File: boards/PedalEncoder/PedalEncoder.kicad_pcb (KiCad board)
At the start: 2 copper layers, 27 parts, among them J1 Pwr, J2 Control, J3 Switch, J4 ISP, J5 Pedal, J6 MIDI Out, Q1 BC547, U1 4069, U2 ATtiny2313V-10P, U3 L7805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

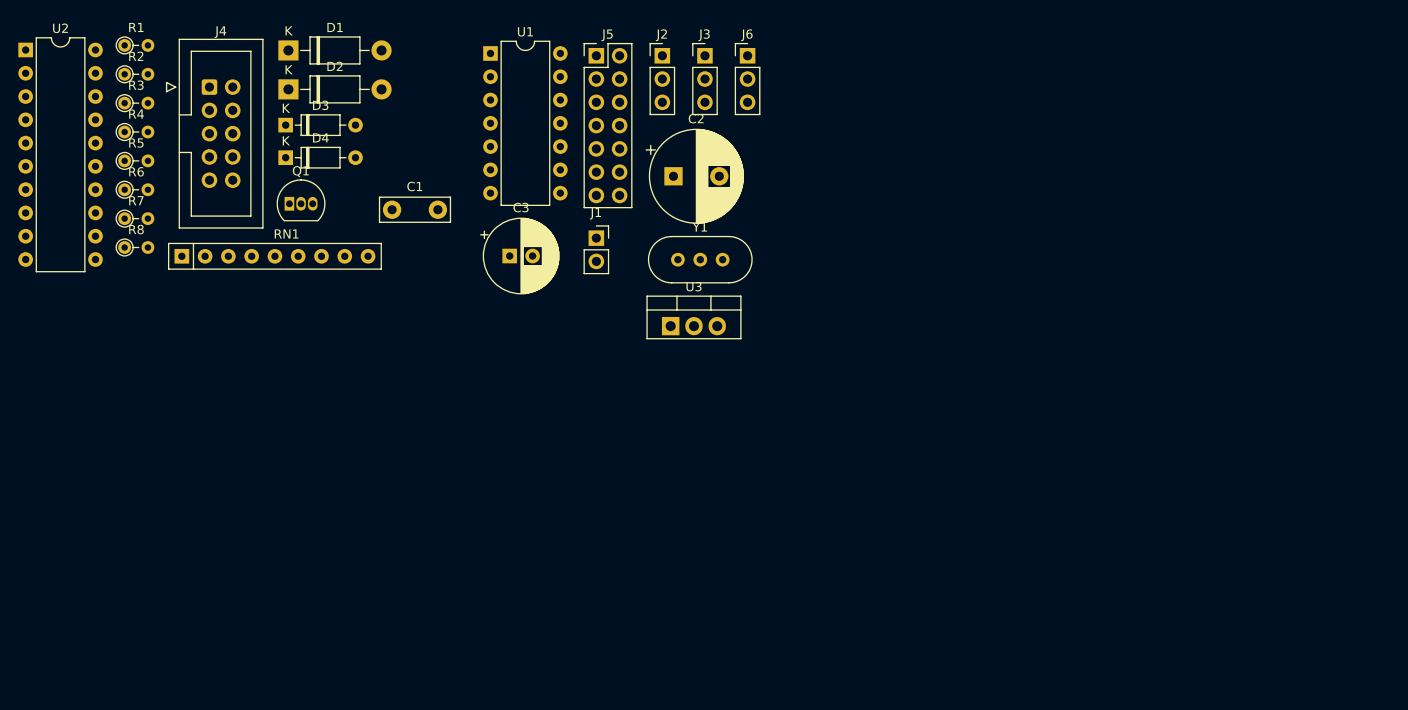
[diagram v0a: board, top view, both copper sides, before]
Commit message: Updated to KiCAD 8, fixed optocouplers for MIDI and added powersupplies
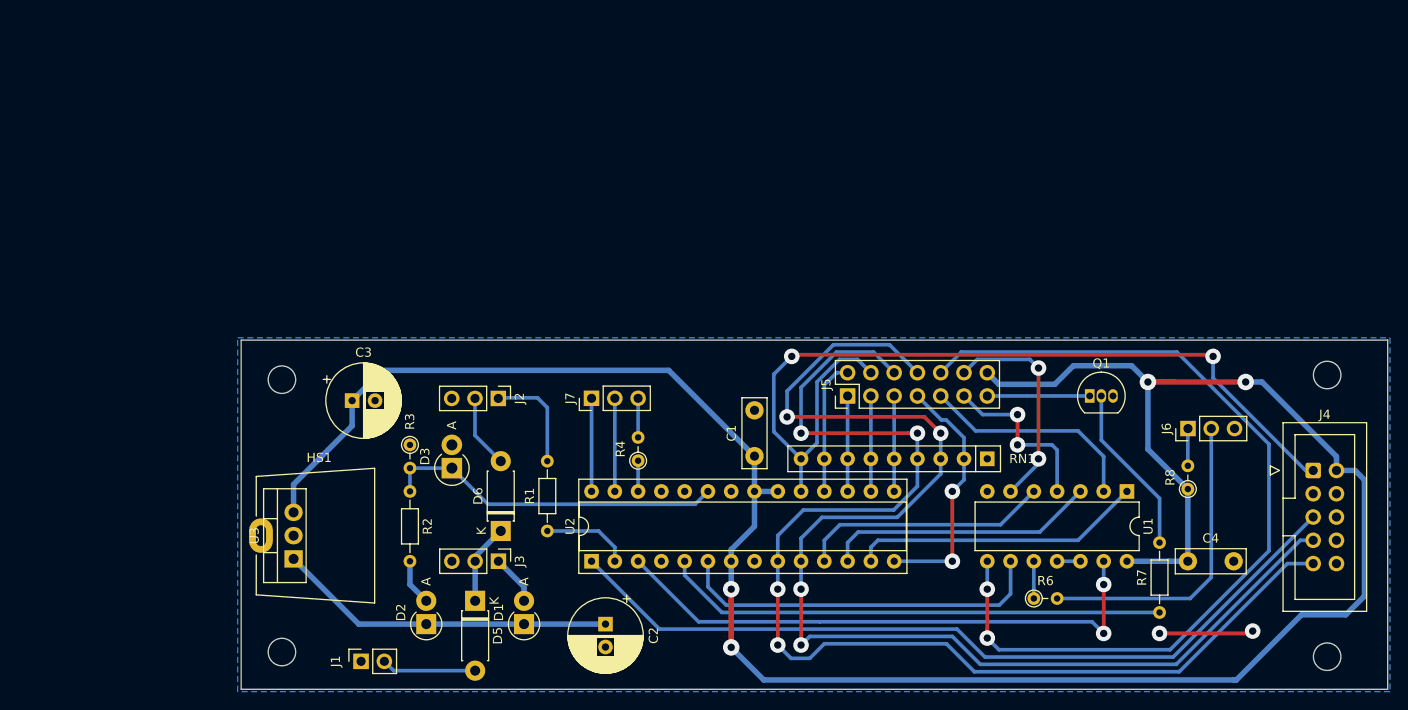
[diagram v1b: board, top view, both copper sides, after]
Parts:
- removed D4: 1N4148, Diode_THT:D_DO-35_SOD27_P7.62mm_Horizontal
- removed R5: 220, Resistor_THT:R_Axial_DIN0204_L3.6mm_D1.6mm_P2.54mm_Vertical
- removed Y1: 4Mhz, Crystal:Crystal_HC49-U-3Pin_Vertical
- added C4: 100nF, Capacitor_THT:C_Disc_D7.5mm_W2.5mm_P5.00mm, F.Cu at (173.3, 99.3)
- added D5: 1N4002, Diode_THT:D_DO-41_SOD81_P7.62mm_Horizontal, F.Cu at (95.5, 103.6)
- added D6: 1N4002, Diode_THT:D_DO-41_SOD81_P7.62mm_Horizontal, F.Cu at (98.3, 96.0)
- added H1: MountingHole, MountingHole:MountingHole_3mm, F.Cu at (74.4, 79.5)
- added H2: MountingHole, MountingHole:MountingHole_3mm, F.Cu at (74.4, 109.2)
- added H3: MountingHole, MountingHole:MountingHole_3mm, F.Cu at (188.5, 79.0)
- added H4: MountingHole, MountingHole:MountingHole_3mm, F.Cu at (188.5, 109.7)
- added HS1: Heatsink_Pad, Heatsink:Heatsink_AAVID_576802B03900G, F.Cu at (72.1, 96.5)
- added J7: I2C, Connector_PinHeader_2.54mm:PinHeader_1x03_P2.54mm_Vertical, F.Cu at (108.2, 81.5)
- C2: value 220uF -> 33uF; footprint Capacitor_THT:CP_Radial_D10.0mm_P5.00mm -> Capacitor_THT:CP_Radial_D8.0mm_P2.50mm
- D1, D2: footprint Diode_THT:D_DO-41_SOD81_P10.16mm_Horizontal -> Diode_THT:D_DO-41_SOD81_P2.54mm_Vertical_AnodeUp
- D3: value 1N4148 -> 4V7; footprint Diode_THT:D_DO-35_SOD27_P7.62mm_Horizontal -> Diode_THT:D_DO-15_P2.54mm_Vertical_AnodeUp
- R1, R7: footprint Resistor_THT:R_Axial_DIN0204_L3.6mm_D1.6mm_P2.54mm_Vertical -> Resistor_THT:R_Axial_DIN0204_L3.6mm_D1.6mm_P7.62mm_Horizontal
- R2: value 220 -> 1k; footprint Resistor_THT:R_Axial_DIN0204_L3.6mm_D1.6mm_P2.54mm_Vertical -> Resistor_THT:R_Axial_DIN0204_L3.6mm_D1.6mm_P7.62mm_Horizontal
- R3: value 220 -> 2k2
- U2: value ATtiny2313V-10P -> ATmega48-20P; footprint Package_DIP:DIP-20_W7.62mm -> Package_DIP:DIP-28_W7.62mm_Socket
- moved J4 127.5 mm to (186.9, 89.4)
- moved R7 120.8 mm to (170.2, 104.9), turned to 90 degrees
- moved R8 119.0 mm to (173.3, 91.4), turned to 90 degrees
- moved R6 108.8 mm to (156.5, 103.4)
- moved RN1 90.6 mm to (151.4, 88.1), turned to 180 degrees
- moved Q1 89.8 mm to (162.6, 81.3)
- moved U1 84.3 mm to (166.6, 91.7), turned to -90 degrees
- moved U2 83.2 mm to (108.2, 99.3), turned to 90 degrees
- moved R1 70.2 mm to (103.4, 96.0), turned to 90 degrees
- moved D1 67.7 mm to (100.8, 106.2), turned to 90 degrees
- moved R4 66.5 mm to (113.3, 88.3), turned to 90 degrees
- moved J6 63.0 mm to (173.3, 84.8), turned to 90 degrees
- moved D2 60.2 mm to (90.2, 106.2), turned to 90 degrees
- moved J3 59.6 mm to (98.0, 99.3), turned to -90 degrees
- moved R2 55.1 mm to (88.4, 91.7), turned to -90 degrees
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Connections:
- net Net-(D1-A) renamed /PWR_ON
- net Net-(D1-K) renamed /PWR_IN
- net Net-(D2-A) renamed /PWR_CFG
- D3 pad 1: RXD -> Config
- D3 pad 2: Net-(D3-A) -> GND
- J1 pad 2: +12V -> Net-(D5-A)
- J2 pad 2: +12V -> Net-(D6-A)
- R1 pad 1: Net-(D4-A) -> RXD
- R2 pad 1: Net-(D3-A) -> Config
- R3 pad 2: Net-(D3-A) -> Config
- R4 pad 1: +5V -> Interrupt
- R4 pad 2: Reset -> Net-(J7-Pin_3)
- RN1 pad 3: Net-(J5-Pin_5) -> SCK
- RN1 pad 4: Net-(J5-Pin_3) -> MISO
- RN1 pad 5: Net-(J5-Pin_1) -> Net-(J5-Pin_5)
- RN1 pad 6: Net-(J5-Pin_2) -> Net-(J5-Pin_3)
- RN1 pad 7: MOSI -> Net-(J5-Pin_1)
- RN1 pad 8: MISO -> Net-(J5-Pin_2)
- RN1 pad 9: SCK -> MOSI
- U1 pad 1: Net-(U2-PD5) -> Net-(U2-PD7)
- U1 pad 3: Net-(U2-PD4) (its old number) -> Net-(U2-PD6)
- U1 pad 5: Net-(U2-PD3) -> Net-(U2-PD5)
- U2 pad 10: GND -> SCK
- U2 pad 11: PWM -> Net-(U2-PD5)
- U2 pad 12: Net-(J5-Pin_7) -> Net-(U2-PD6)
- U2 pad 13: Net-(J5-Pin_5) -> Net-(U2-PD7)
- U2 pad 14: Net-(J5-Pin_3) -> Net-(J5-Pin_7)
- U2 pad 15: Net-(J5-Pin_1) -> Net-(J5-Pin_5)
- U2 pad 16: Net-(J5-Pin_2) -> Net-(J5-Pin_3)
- U2 pad 17: MOSI -> Net-(J5-Pin_1)
- U2 pad 18: MISO -> Net-(J5-Pin_2)
- U2 pad 19: SCK -> MOSI
- U2 pad 4: Net-(U2-PA1/XTAL2) -> unconnected-(U2-PD2-Pad4)
- U2 pad 5: Net-(U2-PA0/XTAL1) -> PWM
- U2 pad 7: Net-(U2-PD3) -> +5V
- U2 pad 8: Net-(U2-PD4) (its old number) -> GND
- U2 pad 9: Net-(U2-PD5) -> MISO
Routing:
- net +5V: track 0.00 -> 252.1 mm, vias 0 -> 4
- net SCK: track 0.00 -> 134.8 mm, vias 0 -> 4
- net MISO: track 0.00 -> 130.9 mm, vias 0 -> 4
- net MOSI: track 0.00 -> 97.0 mm, vias 0 -> 2
- net Net-(J5-Pin_10): track 0.00 -> 96.7 mm, vias 0 -> 2
- net Reset: track 0.00 -> 89.4 mm
- net TXD: track 0.00 -> 61.9 mm, vias 0 -> 2
- net PWM: track 0.00 -> 55.0 mm
- net Net-(U2-PD4): track 0.00 -> 40.7 mm
- net /PWR_IN: track 0.00 -> 37.3 mm
- net Config: track 0.00 -> 37.3 mm
- net Net-(J6-Pin_2): track 0.00 -> 34.0 mm
- net Net-(U2-PD7): track 0.00 -> 32.0 mm
- net Net-(U2-PD6): track 0.00 -> 29.7 mm
- net Net-(J5-Pin_7): track 0.00 -> 27.6 mm, vias 0 -> 2
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- added copper zone on B.Cu, net GND
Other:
- board outline added: 125.1 x 38.1 mm

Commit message: New PCB version of PedalEncoder
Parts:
- D1, D2: footprint Diode_THT:D_DO-41_SOD81_P2.54mm_Vertical_AnodeUp -> Diode_THT:D_DO-41_SOD81_P3.81mm_Vertical_AnodeUp
- D3: footprint Diode_THT:D_DO-15_P2.54mm_Vertical_AnodeUp -> Diode_THT:D_DO-15_P3.81mm_Vertical_AnodeUp
- J1: footprint Connector_PinSocket_2.54mm:PinSocket_1x02_P2.54mm_Vertical -> Connector_PinHeader_2.54mm:PinHeader_1x02_P2.54mm_Vertical
- Q1: footprint Package_TO_SOT_THT:TO-92_Inline -> Package_TO_SOT_THT:TO-92_Inline_Wide
- moved Q1 2.54 mm to (160.0, 81.3)
- moved D2 1.78 mm to (88.4, 106.2)
- moved D1 1.52 mm to (102.4, 106.2)
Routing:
- net GND: track 10.3 -> 55.6 mm, vias 2 -> 10
- net Net-(Q1-B): track 18.6 -> 26.5 mm
- net LED: track 11.2 -> 8.64 mm
- net /PWR_CFG: track 5.05 -> 7.11 mm
- net Net-(J6-Pin_2): track 34.0 -> 32.8 mm
- net Net-(J5-Pin_7): track 27.6 -> 26.5 mm

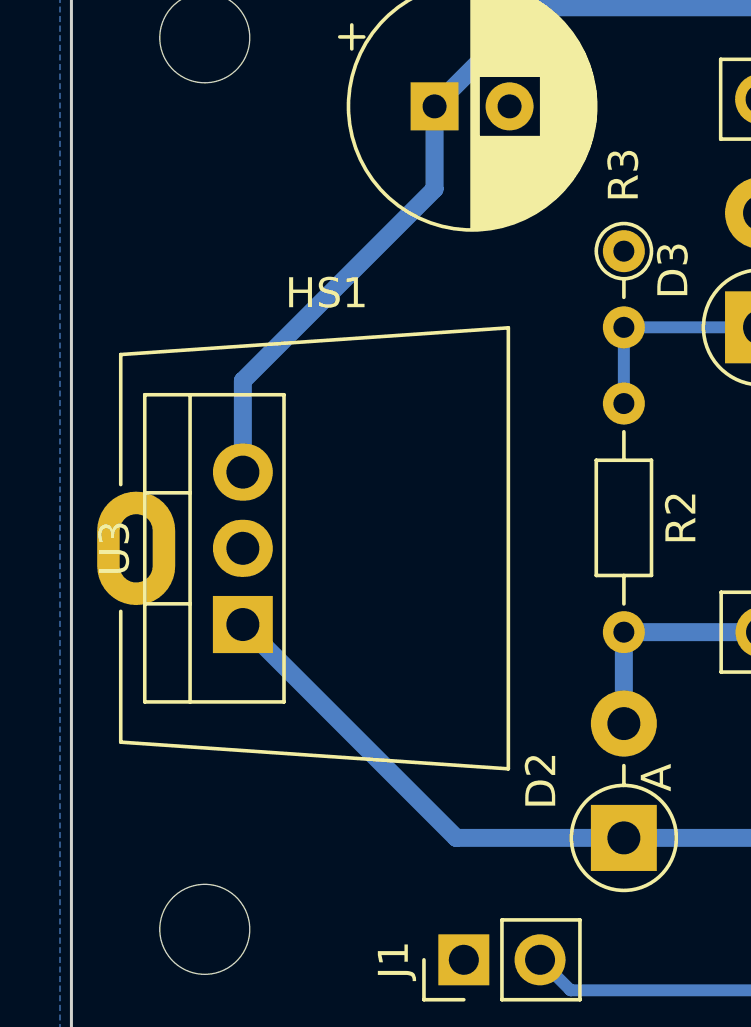
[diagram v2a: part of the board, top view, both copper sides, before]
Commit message: Using custom TO220 cooler, fixed and finished several PCBs
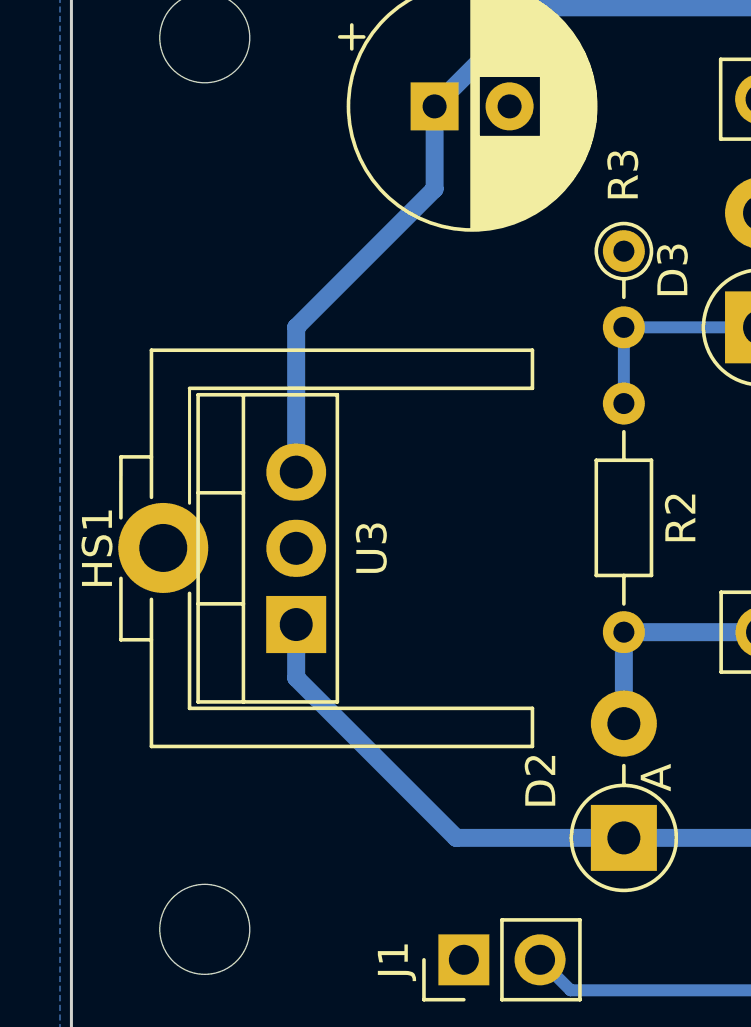
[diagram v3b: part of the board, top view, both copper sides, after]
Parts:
- HS1: footprint Heatsink:Heatsink_AAVID_576802B03900G -> Custom_Heatsinks:Heatsink_Aavid_TO-220_H12.7mm
- moved HS1 1.78 mm to (73.9, 96.5), turned to 90 degrees
- moved U3 1.78 mm to (77.5, 99.1)
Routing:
- net /PWR_IN: track 37.0 -> 36.2 mm
- net +5V: track 252.1 -> 251.3 mm
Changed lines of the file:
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@@
 		)
 	)
-	(footprint "Heatsink:Heatsink_AAVID_576802B03900G"
+	(footprint "Custom_Heatsinks:Heatsink_Aavid_TO-220_H12.7mm"
 		(layer "F.Cu")
-		(at 72.136 96.52)
-		(descr "Heatsink, 14.48x12.7x19.05mm, TO-220/ TO-262, https://www.boydcorp.com/aavid-datasheets/Board-Level-Cooling-Plug-In-5768.pdf")
-		(tags "heatsink")
+		(at 73.914 96.52 90)
 		(property "Reference" "HS1"
-			(at 6.35 -8.5 0)
+			(at 0 -3.048 270)
 			(layer "F.SilkS")
 			(effects
@@
 		)
 		(property "Value" "Heatsink_Pad"
-			(at 6.35 8.5 0)
+			(at 0 12.446 270)
 			(layer "F.Fab")
 			(effects
@@
 			)
 		)
-		(property "Footprint" "Heatsink:Heatsink_AAVID_576802B03900G"
-			(at 0 0 0)
+		(property "Footprint" "Custom_Heatsinks:Heatsink_Aavid_TO-220_H12.7mm"
+			(at 0 0 90)
 			(unlocked yes)
 			(layer "F.Fab")
@@
 		)
 		(property "Datasheet" ""
-			(at 0 0 0)
+			(at 0 0 90)
 			(unlocked yes)
 			(layer "F.Fab")
@@
 		)
 		(property "Description" "Heatsink with electrical connection, 1 pin"
-			(at 0 0 0)
+			(at 0 0 90)
 			(unlocked yes)
 			(layer "F.Fab")
@@
 		(attr through_hole)
 		(fp_line
-			(start -0.515 -6.46)
-			(end -0.515 -2.125)
+			(start 3.048 -2.286)
+			(end 1.017015 -2.287308)
 			(stroke
 				(width 0.12)
-				(type solid)
+				(type default)
 			)
 			(layer "F.SilkS")
 		)
 		(fp_line
-			(start -0.515 -6.46)
-			(end 12.405 -7.35)
+			(start 3.048 -2.286)
+			(end 3.048 -1.27)
 			(stroke
 				(width 0.12)
@@
 		)
 		(fp_line
-			(start -0.515 2.1)
-			(end -0.515 6.46)
+			(start -3.048 -2.286)
+			(end -1 -2.286)
 			(stroke
 				(width 0.12)
@@
 		)
 		(fp_line
-			(start -0.515 6.46)
-			(end 12.405 7.35)
+			(start 6.604 -1.27)
+			(end 1.7 -1.269522)
 			(stroke
 				(width 0.12)
-				(type solid)
+				(type default)
 			)
 			(layer "F.SilkS")
 		)
 		(fp_line
-			(start 12.405 -7.35)
-			(end 12.405 7.35)
+			(start -1.7 -1.27)
+			(end -6.604 -1.27)
 			(stroke
 				(width 0.12)
@@
 		)
 		(fp_line
-			(start 0.405 -1.85)
-			(end 1.675 -1.85)
-			(stroke
-				(width 0.1)
-				(type solid)
-			)
-			(layer "Dwgs.User")
-		)
-		(fp_line
-			(start 0.405 1.85)
-			(end 1.675 1.85)
-			(stroke
-				(width 0.1)
-				(type solid)
-			)
-			(layer "Dwgs.User")
-		)
-		(fp_line
-			(start 0.45 -5)
-			(end 4.45 -5)
-			(stroke
-				(width 0.1)
-				(type solid)
-			)
-			(layer "Dwgs.User")
-		)
-		(fp_line
-			(start 1.675 -5)
-			(end 1.675 5)
-			(stroke
-				(width 0.1)
-				(type solid)
-			)
-			(layer "Dwgs.User")
-		)
-		(fp_line
-			(start 4.45 -5)
-			(end 4.45 5)
-			(stroke
-				(width 0.1)
-				(type solid)
-			)
-			(layer "Dwgs.User")
-		)
-		(fp_line
-			(start 4.45 5)
-			(end 0.45 5)
+			(start -3.048 -1.27)
+			(end -3.048 -2.286)
 			(stroke
-				(width 0.1)
-				(type solid)
-			)
-			(layer "Dwgs.User")
-		)
-		(fp_line
-			(start -1.55 -7.49)
-			(end -1.55 7.49)
-			(stroke
-				(width 0.05)
-				(type solid)
-			)
-			(layer "F.CrtYd")
-		)
-		(fp_line
-			(start -1.55 7.49)
-			(end 12.55 7.49)
-			(stroke
-				(width 0.05)
-				(type solid)
-			)
-			(layer "F.CrtYd")
-		)
-		(fp_line
-			(start 12.55 -7.49)
-			(end -1.55 -7.49)
-			(stroke
-				(width 0.05)
+				(width 0.12)
 				(type solid)
 			)
-			(layer "F.CrtYd")
+			(layer "F.SilkS")
 		)
 		(fp_line
-			(start 12.55 -7.49)
-			(end 12.55 7.49)
+			(start -6.604 -1.27)
+			(end -6.604 11.43)
 			(stroke
-				(width 0.05)
+				(width 0.12)
 				(type solid)
 			)
-			(layer "F.CrtYd")
+			(layer "F.SilkS")
 		)
 		(fp_line
-			(start -0.405 -6.35)
-			(end -0.405 6.35)
+			(start 5.334 0)
+			(end 5.334 11.43)
 			(stroke
-				(width 0.1)
+				(width 0.12)
 				(type solid)
 			)
-			(layer "F.Fab")
+			(layer "F.SilkS")
 		)
 		(fp_line
-			(start -0.405 -6.35)
-			(end 12.295 -7.24)
+			(start 1.5 0)
+			(end 5.334 0)
 			(stroke
 				(width 0.1)
-				(type solid)
+				(type default)
 			)
-			(layer "F.Fab")
+			(layer "F.SilkS")
 		)
 		(fp_line
-			(start 0.405 -5.597)
-			(end 0.405 5.597)
+			(start -5.334 0)
+			(end -1.5 0)
 			(stroke
-				(width 0.1)
+				(width 0.12)
 				(type solid)
 			)
-			(layer "F.Fab")
+			(layer "F.SilkS")
 		)
 		(fp_line
-			(start 0.405 -5.597)
-			(end 12.295 -6.43)
+			(start 6.604 11.43)
+			(end 6.604 -1.27)
 			(stroke
-				(width 0.1)
+				(width 0.12)
 				(type solid)
 			)
-			(layer "F.Fab")
+			(layer "F.SilkS")
 		)
 		(fp_line
-			(start 12.295 -7.24)
-			(end 12.295 7.24)
+			(start 5.334 11.43)
+			(end 6.604 11.43)
 			(stroke
-				(width 0.1)
+				(width 0.12)
 				(type solid)
 			)
-			(layer "F.Fab")
+			(layer "F.SilkS")
 		)
 		(fp_line
-			(start 12.295 7.24)
-			(end -0.405 6.35)
+			(start -5.334 11.43)
+			(end -5.334 0)
 			(stroke
-				(width 0.1)
+				(width 0.12)
 				(type solid)
 			)
-			(layer "F.Fab")
+			(layer "F.SilkS")
 		)
 		(fp_line
-			(start 12.3 6.43)
-			(end 0.405 5.597)
+			(start -6.604 11.43)
+			(end -5.334 11.43)
 			(stroke
-				(width 0.1)
+				(width 0.12)
 				(type solid)
 			)
-			(layer "F.Fab")
-		)
-		(fp_text user "${REFERENCE}"
-			(at 6.35 0 0)
-			(layer "F.Fab")
-			(effects
-				(font
-					(size 1 1)
-					(thickness 0.15)
-				)
-			)
+			(layer "F.SilkS")
 		)
-		(pad "1" thru_hole oval
-			(at 0 0)
-			(size 2.6 3.78)
-			(drill oval 1.1 2.28)
+		(pad "1" thru_hole circle
+			(at 0.0127 -0.8763 90)
+			(size 3 3)
+			(drill 1.6)
 			(layers "*.Cu" "*.Mask")
 			(remove_unused_layers no)
 			(net 33 "unconnected-(HS1-Pad1)")
 			(pintype "passive+no_connect")
-		)
-		(model "${KICAD8_3DMODEL_DIR}/Heatsink.3dshapes/Heatsink_AAVID_576802B03900G.wrl"
-			(offset
-				(xyz 0 0 0)
-			)
-			(scale
-				(xyz 1 1 1)
-			)
-			(rotate
-				(xyz 0 0 0)
-			)
+			(clearance 0.3)
+			(zone_connect 1)
 		)
 	)
@@
 	(footprint "Package_TO_SOT_THT:TO-220-3_Vertical"
 		(layer "F.Cu")
-		(at 75.692 99.06 90)
+		(at 77.47 99.06 90)
 		(descr "TO-220-3, Vertical, RM 2.54mm, see https://www.vishay.com/docs/66542/to-220-1.pdf")
 		(tags "TO-220-3 Vertical RM 2.54mm")
 		(property "Reference" "U3"
-			(at 2.54 -4.27 -90)
+			(at 2.54 2.54 -90)
 			(layer "F.SilkS")
 			(effects
@@
 	)
 	(segment
-		(start 75.692 93.98)
-		(end 75.692 90.932)
+		(start 77.47 93.98)
+		(end 77.47 89.154)
 		(width 0.6)
 		(layer "B.Cu")
@@
 	)
 	(segment
-		(start 75.692 90.932)
-		(end 82.082 84.542)
+		(start 126.998 112.266)
+		(end 178.308 112.266)
 		(width 0.6)
 		(layer "B.Cu")
@@
 	)
 	(segment
-		(start 126.998 112.266)
-		(end 178.308 112.266)
+		(start 85.384 78.486)
+		(end 116.626 78.486)
 		(width 0.6)
 		(layer "B.Cu")
@@
 	)
 	(segment
-		(start 85.384 78.486)
-		(end 116.626 78.486)
+		(start 77.47 89.154)
+		(end 82.082 84.542)
 		(width 0.6)
 		(layer "B.Cu")
@@
 	)
 	(segment
-		(start 75.692 99.06)
+		(start 77.47 100.838)
 		(end 82.804 106.172)
 		(width 0.6)
 		(layer "B.Cu")
+		(net 43)
+	)
+	(segment
+		(start 77.47 99.06)
+		(end 77.47 100.838)
+		(width 0.6)
+		(layer "B.Cu")
